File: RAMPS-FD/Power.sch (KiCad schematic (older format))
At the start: 22 parts, among them J1 NET-TIE, P101 HB_IN, P105 12V-AUX, P107 MOT_IN, P108 POWER_IN, P219 EXT_5V, U3 LM7812, U4 L7805CV-DG

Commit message: Changed fuse holders to Keystone 3568; specificy HCT instead of ACT logic
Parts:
- removed P107: MOT_IN, w_conn_screw:mstba_2,5%2f2-g-5,08, symbol CONN_2
- C102: value 100n 35V -> 100n 50V
- C207, C3: value 100n 16V -> 100n
- D102: value SS10Pxx -> V10P10
- D103: symbol DIODE -> D
- F101, F102, F103: footprint rmc:FUSE-MINI-AUTO -> rmc:Keystone_3568
- J1: Populate (none) -> No
- JP101, JP102: footprint w_pin_strip:pin_strip_3 -> Pin_Headers:Pin_Header_Straight_1x03
- JP201: footprint w_pin_strip:pin_strip_2 -> Pin_Headers:Pin_Header_Straight_1x02
- P108: footprint w_conn_screw:mstba_2,5%2f2-g-5,08 -> w_conn_screw:mstba_2,5%2f4-g-5,08; symbol CONN_2 -> CONN_4
- U4: symbol LM7812 -> LM7805
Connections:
- net +12P: now also D103.2 (A); no longer D103.1 (A)
- net GNDPWR: now also P108.3 (P3)
- net LP_1: now also D103.1 (K); no longer D103.2 (K)
- net MOT_IN: now also P108.4 (P4)
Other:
- note added: "Capacitors rated to at least 25V \nunless otherwise stated"
- note added: "or equivalent"
- note removed: "or equiv V10P"
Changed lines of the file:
@@
 F 0 "JP102" H 2850 5000 60  0000 C CNN
 F 1 "VSEL" H 2850 4875 60  0000 C CNN
-F 2 "w_pin_strip:pin_strip_3" H 2850 4700 60  0001 C CNN
+F 2 "Pin_Headers:Pin_Header_Straight_1x03" H 2850 4700 60  0001 C CNN
 F 3 "" H 2850 4700 60  0001 C CNN
 	1    2850 4700
@@
 $EndComp
 $Comp
-L CONN_2 P108
+L CONN_4 P108
 U 1 1 51AA108A
-P 4350 3100
-F 0 "P108" V 4300 3100 40  0000 C CNN
-F 1 "POWER_IN" V 4400 3100 40  0000 C CNN
-F 2 "w_conn_screw:mstba_2,5%2f2-g-5,08" H 4350 3100 60  0001 C CNN
-F 3 "" H 4350 3100 60  0001 C CNN
-	1    4350 3100
+P 4100 2500
+F 0 "P108" V 4050 2500 40  0000 C CNN
+F 1 "POWER_IN" V 4150 2500 40  0000 C CNN
+F 2 "w_conn_screw:mstba_2,5%2f4-g-5,08" H 4100 2500 60  0001 C CNN
+F 3 "" H 4100 2500 60  0001 C CNN
+	1    4100 2500
 	-1   0    0    1
 $EndComp
@@
 Text GLabel 3025 7450 2    50   Input ~ 0
 PS-ON
-Text Notes 1850 3025 0    60   ~ 0
+Text Notes 1650 2875 0    60   ~ 0
 Medium power MOSFETS \n(extruder heaters, fans)
 Text Notes 2000 1300 0    60   ~ 0
 Heatbed Only: 12-24V, 15A
-Text Notes 2300 2150 0    60   ~ 0
+Text Notes 2300 2050 0    60   ~ 0
 Motors only,  12-24V
 $Comp
@@
 F 0 "JP101" V 5050 7350 60  0000 C CNN
 F 1 "VLOG" V 5150 7325 60  0000 C CNN
-F 2 "w_pin_strip:pin_strip_3" H 5100 7050 60  0001 C CNN
+F 2 "Pin_Headers:Pin_Header_Straight_1x03" H 5100 7050 60  0001 C CNN
 F 3 "" H 5100 7050 60  0001 C CNN
 	1    5100 7050
@@
 F 0 "F103" H 5350 1950 40  0000 C CNN
 F 1 "FUSE 10A" H 5400 2150 40  0000 C CNN
-F 2 "rmc:FUSE-MINI-AUTO" H 5450 2000 60  0001 C CNN
+F 2 "rmc:Keystone_3568" H 5450 2000 60  0001 C CNN
 F 3 "" H 5450 2000 60  0001 C CNN
 	1    5450 2000
@@
 $EndComp
 $Comp
-L CONN_2 P107
-U 1 1 5176E748
-P 4350 2100
-F 0 "P107" V 4300 2100 40  0000 C CNN
-F 1 "MOT_IN" V 4400 2100 40  0000 C CNN
-F 2 "w_conn_screw:mstba_2,5%2f2-g-5,08" H 4350 2100 60  0001 C CNN
-F 3 "" H 4350 2100 60  0001 C CNN
-	1    4350 2100
-	-1   0    0    1
-$EndComp
-$Comp
 L CONN_2 P105
 U 1 1 50FC30EF
@@
 AR Path="/5239FE5C/50FC27BF" Ref="C102"  Part="1"
 F 0 "C102" H 7150 3400 50  0000 L CNN
-F 1 "100n 35V" H 7150 3200 50  0000 L CNN
+F 1 "100n 50V" H 7150 3200 50  0000 L CNN
 F 2 "Capacitors_SMD:C_0603" H 7100 3300 60  0001 C CNN
 F 3 "" H 7100 3300 60  0001 C CNN
@@
 $EndComp
 $Comp
-L DIODE D103
+L D D103
 U 1 1 50FC273D
 P 3200 5500
@@
 F 3 "" H 3200 5500 60  0001 C CNN
 	1    3200 5500
-	1    0    0    -1
+	-1   0    0    1
 $EndComp
 $Comp
@@
 F 0 "F102" H 5350 2900 40  0000 C CNN
 F 1 "FUSE 10A" H 5400 3100 40  0000 C CNN
-F 2 "rmc:FUSE-MINI-AUTO" H 5450 3000 60  0001 C CNN
+F 2 "rmc:Keystone_3568" H 5450 3000 60  0001 C CNN
 F 3 "" H 5450 3000 60  0001 C CNN
 	1    5450 3000
@@
 F 0 "F101" H 5350 1050 40  0000 C CNN
 F 1 "FUSE 15A" H 5400 1300 40  0000 C CNN
-F 2 "rmc:FUSE-MINI-AUTO" H 5450 1150 60  0001 C CNN
+F 2 "rmc:Keystone_3568" H 5450 1150 60  0001 C CNN
 F 3 "" H 5450 1150 60  0001 C CNN
 	1    5450 1150
@@
 AR Path="/5239FE5C/523F9247" Ref="C207"  Part="1"
 F 0 "C207" H 2550 5150 50  0000 L CNN
-F 1 "100n 16V" H 2550 4950 50  0000 L CNN
+F 1 "100n" H 2550 4950 50  0000 L CNN
 F 2 "Capacitors_SMD:C_0603" H 2500 5050 60  0001 C CNN
 F 3 "" H 2500 5050 60  0001 C CNN
@@
 Text Notes 9300 2500 0    60   ~ 0
 Note: use thick traces for all\nhigh power connections
-Text Notes 1850 3375 0    60   ~ 0
+Text Notes 1650 3225 0    60   ~ 0
 12V or 24V input \n(ensure to set JP102 correctly!)
 Text GLabel 3375 6775 1    50   Input ~ 0
@@
 F 0 "JP201" H 3700 6825 60  0000 C CNN
 F 1 "5V_SEL" H 3675 6725 60  0000 C CNN
-F 2 "w_pin_strip:pin_strip_2" H 3700 6900 60  0001 C CNN
+F 2 "Pin_Headers:Pin_Header_Straight_1x02" H 3700 6900 60  0001 C CNN
 F 3 "~" H 3700 6900 60  0000 C CNN
 	1    3700 6900
@@
 P 6100 3350
 F 0 "D102" H 6100 3050 60  0000 C CNN
-F 1 "SS10Pxx" V 6500 3200 60  0000 C CNN
+F 1 "V10P10" V 6500 3200 60  0000 C CNN
 F 2 "rmc:TO277A_RMC" H 6100 3350 60  0001 C CNN
 F 3 "" H 6100 3350 60  0000 C CNN
@@
 $EndComp
 Text Notes 5650 4000 0    60   ~ 0
-or equiv V10P
-$Comp
-L LM7812 U4
+or equivalent
+$Comp
+L LM7805 U4
 U 1 1 571CC545
 P 7800 5000
@@
 AR Path="/5239FE5C/571CC57E" Ref="C3"  Part="1"
 F 0 "C3" H 7050 5350 50  0000 L CNN
-F 1 "100n 16V" H 7050 5150 50  0000 L CNN
+F 1 "100n" H 7050 5150 50  0000 L CNN
 F 2 "Capacitors_SMD:C_0603" H 7000 5250 60  0001 C CNN
 F 3 "" H 7000 5250 60  0001 C CNN
@@
 F 3 "" H 8175 3650 60  0000 C CNN
 F 4 "Copper jumper block" H 8195 3270 60  0001 C CNN "Description"
+F 5 "No" H 8175 3650 60  0001 C CNN "Populate"
 	1    8175 3650
 	1    0    0    -1
@@
 	7600 3650 7600 3750
 Wire Wire Line
-	4850 3650 7975 3650
-Wire Wire Line
-	4700 2200 7900 2200
+	4450 3650 7975 3650
+Wire Wire Line
+	4600 2200 7900 2200
 Wire Wire Line
 	8500 3625 8500 3750
@@
 Connection ~ 5500 7050
 Wire Notes Line
-	4200 3100 3400 3100
-Wire Notes Line
-	4200 2100 3350 2100
+	4550 3000 3200 3000
+Wire Notes Line
+	4350 2000 3350 2000
 Wire Wire Line
 	5500 7050 5500 6900
@@
 	10050 5950 10400 5950
 Wire Wire Line
-	5200 2000 4700 2000
+	4450 2000 5200 2000
 Wire Wire Line
 	6450 1800 6450 2000
@@
 	7100 3000 7100 3150
 Connection ~ 6050 3000
-Wire Wire Line
-	4850 3650 4850 3200
 Connection ~ 6400 1150
 Wire Wire Line
@@
 	5700 1150 6600 1150
 Wire Wire Line
-	5200 3000 4700 3000
-Wire Wire Line
-	4850 3200 4700 3200
+	5200 3000 4600 3000
 Connection ~ 6050 3650
 Wire Wire Line
@@
 	3350 1250 4200 1250
 Wire Wire Line
-	3800 5500 3400 5500
+	3800 5500 3350 5500
 Connection ~ 7350 3000
 Wire Wire Line
@@
 	800  4700 1600 4700
 Wire Wire Line
-	2850 5500 3000 5500
+	2850 5500 3050 5500
 Wire Wire Line
 	3000 4700 3200 4700
@@
 	3350 1350 1900 1350
 Wire Notes Line
-	2250 2000 3350 2000
-Wire Notes Line
-	3350 2000 3350 2200
-Wire Notes Line
-	3350 2200 2250 2200
-Wire Notes Line
-	3400 3500 3400 2800
-Wire Notes Line
-	1700 3500 3400 3500
+	2250 1900 3350 1900
+Wire Notes Line
+	3350 1900 3350 2100
+Wire Notes Line
+	3350 2100 2250 2100
+Wire Notes Line
+	3200 3350 3200 2650
+Wire Notes Line
+	1500 3350 3200 3350
 Wire Wire Line
 	2850 4800 2850 5500
@@
 	1900 1350 1900 1150
 Wire Notes Line
-	2250 2200 2250 2000
-Wire Notes Line
-	1700 3500 1700 2800
-Wire Notes Line
-	1700 2800 3400 2800
+	2250 2100 2250 1900
+Wire Notes Line
+	1500 3350 1500 2650
+Wire Notes Line
+	1500 2650 3200 2650
 Wire Notes Line
 	6800 5400 4600 5400
@@
 Wire Notes Line
 	6150 6650 5200 6650
+Wire Wire Line
+	4450 2350 4450 2000
+Wire Wire Line
+	4450 2450 4600 2450
+Wire Wire Line
+	4600 2450 4600 2200
+Wire Wire Line
+	4600 3000 4600 2550
+Wire Wire Line
+	4600 2550 4450 2550
+Wire Wire Line
+	4450 2650 4450 3650
+Text Notes 9550 4700 0    60   ~ 0
+Capacitors rated to at least 25V \nunless otherwise stated
 $EndSCHEMATC

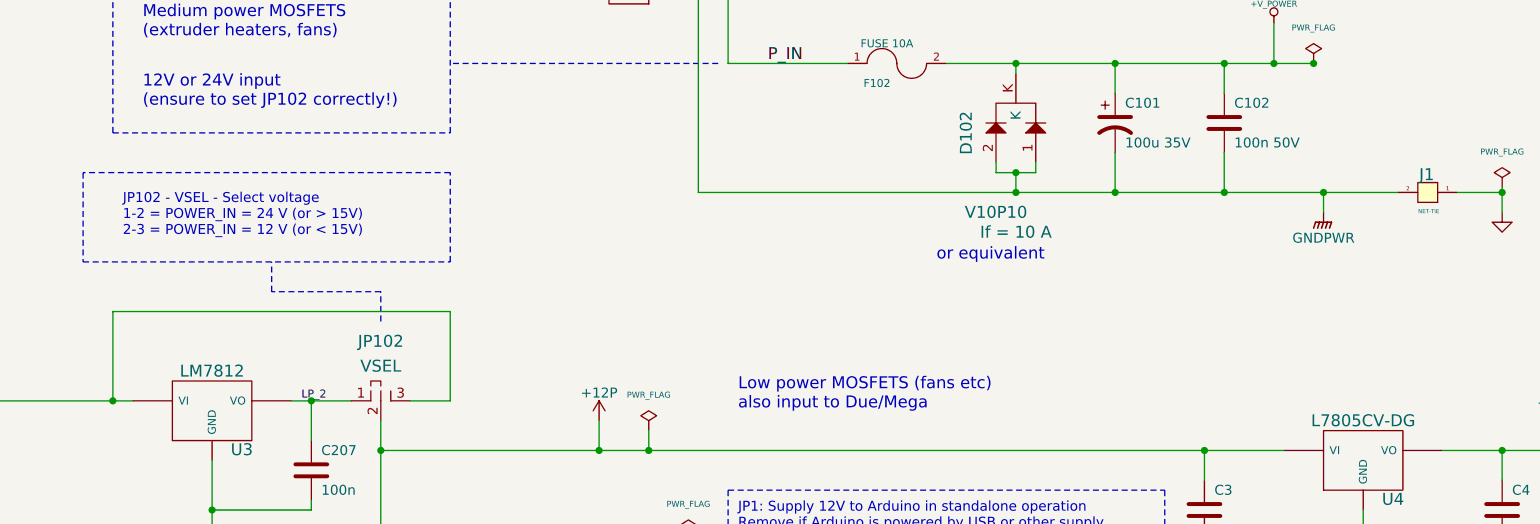
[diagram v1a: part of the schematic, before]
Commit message: Fix 3d view; remove faulty ADC protection
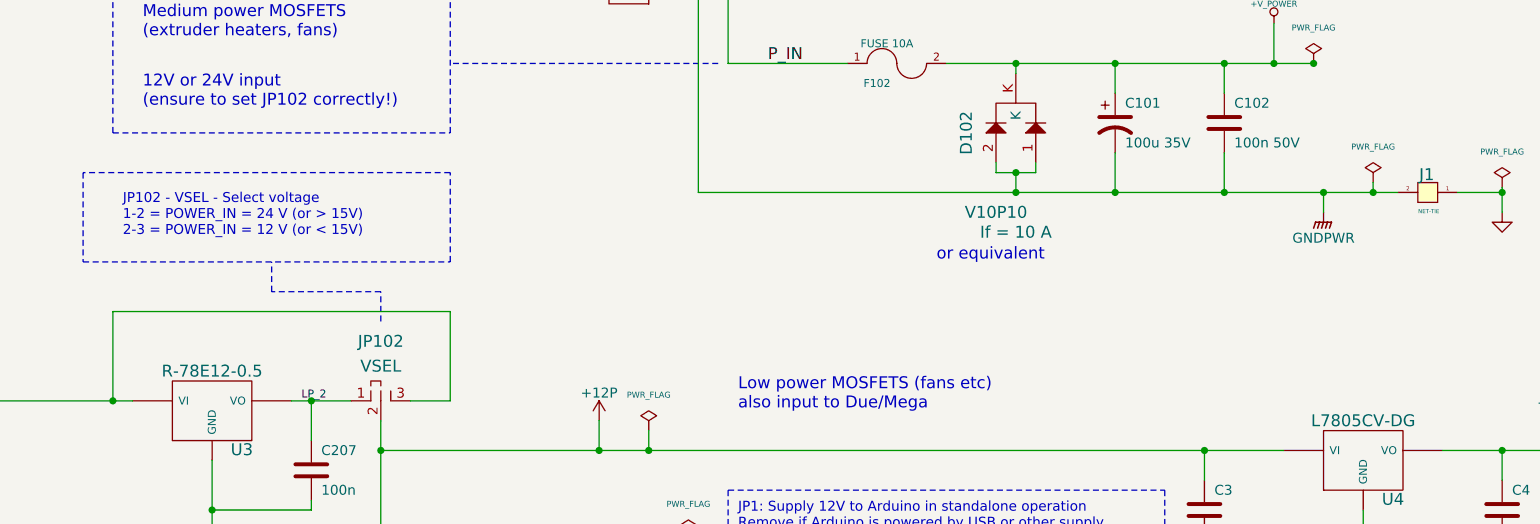
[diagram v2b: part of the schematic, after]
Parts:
- C101: footprint Capacitors_SMD:c_elec_6.3x7.7 -> Capacitors_SMD:CP_Elec_6.3x7.7
- JP1, JP201: footprint Pin_Headers:Pin_Header_Straight_1x02 -> Pin_Headers:Pin_Header_Straight_1x02_Pitch2.54mm
- JP101, JP102: footprint Pin_Headers:Pin_Header_Straight_1x03 -> Pin_Headers:Pin_Header_Straight_1x03_Pitch2.54mm
- U3: value LM7812 -> R-78E12-0.5
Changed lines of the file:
@@
 F 0 "JP102" H 2850 5000 60  0000 C CNN
 F 1 "VSEL" H 2850 4875 60  0000 C CNN
-F 2 "Pin_Headers:Pin_Header_Straight_1x03" H 2850 4700 60  0001 C CNN
+F 2 "Pin_Headers:Pin_Header_Straight_1x03_Pitch2.54mm" H 2850 4700 60  0001 C CNN
 F 3 "" H 2850 4700 60  0001 C CNN
 	1    2850 4700
@@
 F 0 "JP1" H 3950 5400 60  0000 C CNN
 F 1 "VIN" H 3950 5300 60  0000 C CNN
-F 2 "Pin_Headers:Pin_Header_Straight_1x02" H 3950 5500 60  0001 C CNN
+F 2 "Pin_Headers:Pin_Header_Straight_1x02_Pitch2.54mm" H 3950 5500 60  0001 C CNN
 F 3 "" H 3950 5500 60  0001 C CNN
 	1    3950 5500
@@
 F 0 "JP101" V 5050 7350 60  0000 C CNN
 F 1 "VLOG" V 5150 7325 60  0000 C CNN
-F 2 "Pin_Headers:Pin_Header_Straight_1x03" H 5100 7050 60  0001 C CNN
+F 2 "Pin_Headers:Pin_Header_Straight_1x03_Pitch2.54mm" H 5100 7050 60  0001 C CNN
 F 3 "" H 5100 7050 60  0001 C CNN
 	1    5100 7050
@@
 F 0 "C101" H 6600 3400 50  0000 L CNN
 F 1 "100u 35V" H 6600 3200 50  0000 L CNN
-F 2 "Capacitors_SMD:c_elec_6.3x7.7" H 6550 3300 60  0001 C CNN
+F 2 "Capacitors_SMD:CP_Elec_6.3x7.7" H 6550 3300 60  0001 C CNN
 F 3 "" H 6550 3300 60  0001 C CNN
 	1    6550 3300
@@
 P 2000 4750
 F 0 "U3" H 2150 4554 60  0000 C CNN
-F 1 "LM7812" H 2000 4950 60  0000 C CNN
+F 1 "R-78E12-0.5" H 2000 4950 60  0000 C CNN
 F 2 "discret:LM78XXV" H 2000 4750 60  0001 C CNN
 F 3 "~" H 2000 4750 60  0000 C CNN
@@
 F 0 "JP201" H 3700 6825 60  0000 C CNN
 F 1 "5V_SEL" H 3675 6725 60  0000 C CNN
-F 2 "Pin_Headers:Pin_Header_Straight_1x02" H 3700 6900 60  0001 C CNN
+F 2 "Pin_Headers:Pin_Header_Straight_1x02_Pitch2.54mm" H 3700 6900 60  0001 C CNN
 F 3 "~" H 3700 6900 60  0000 C CNN
 	1    3700 6900
@@
 	1    0    0    -1
 $EndComp
+Text Notes 3850 6225 0    60   Italic 0
+Arduino base board
+Text Notes 5375 6525 0    50   ~ 0
+Note: On R3 compatible Arduinos, IOREF \nwill supply 3.3V (Due), or 5V (Mega).\n\nIf IOREF is not provided (non-R3) then it \nmust be a 5V Arduino so set VLOG to 5V.
+Text Notes 9550 4700 0    60   ~ 0
+Capacitors rated to at least 25V \nunless otherwise stated
 Connection ~ 2850 4950
 Connection ~ 3950 4950
@@
 Wire Wire Line
 	4925 5500 4925 5525
-Text Notes 3850 6225 0    60   Italic 0
-Arduino base board
 Wire Wire Line
 	3375 6775 3375 6900
@@
 Wire Notes Line
 	5350 6550 7000 6550
-Text Notes 5375 6525 0    50   ~ 0
-Note: On R3 compatible Arduinos, IOREF \nwill supply 3.3V (Due), or 5V (Mega).\n\nIf IOREF is not provided (non-R3) then it \nmust be a 5V Arduino so set VLOG to 5V.
 Wire Notes Line
 	5350 6100 7000 6100
@@
 Wire Wire Line
 	4450 2650 4450 3650
-Text Notes 9550 4700 0    60   ~ 0
-Capacitors rated to at least 25V \nunless otherwise stated
+$Comp
+L PWR_FLAG #FLG035
+U 1 1 5B126588
+P 7850 3600
+F 0 "#FLG035" H 7850 3695 30  0001 C CNN
+F 1 "PWR_FLAG" H 7850 3780 30  0000 C CNN
+F 2 "" H 7850 3600 60  0001 C CNN
+F 3 "" H 7850 3600 60  0001 C CNN
+	1    7850 3600
+	1    0    0    -1
+$EndComp
+Wire Wire Line
+	7850 3600 7850 3650
+Connection ~ 7850 3650
 $EndSCHEMATC
